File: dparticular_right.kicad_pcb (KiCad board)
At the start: 2 copper layers, 185.7 x 157.2 mm, 51 parts, among them J1 To Left Hand, SW1:10 Key_Ins, SW1:11 Key_Prnt, SW2:10 Key_F7, SW2:11 Key_F8, SW2:12 Key_F9, SW2:13 Key_F10, SW2:14 Key_F11, SW2:15 Key_F12, SW2:16 Key_Del, SW3:10 Key_7, SW3:11 Key_8, SW3:12 Key_9, SW3:13 Key_0, SW3:14 Key_Hyph, SW3:15 Key_Eql, SW3:16 Key_Bksp, SW3:9 Key_6, SW4:10 Key_U, SW4:11 Key_I, SW4:12 Key_O, SW4:13 Key_P, SW4:14 Key_LBrk, SW4:15 Key_RBrk, SW4:16 Key_BkSl, SW4:9 Key_Y, SW5:10 Key_J, SW5:11 Key_K, SW5:12 Key_L, SW5:13 Key_Semi, SW5:14 Key_Quot, SW5:16 Key_Entr, SW5:9 Key_H, SW6:10 Key_M, SW6:11 Key_Coma, SW6:12 Key_Per, SW6:13 Key_Slsh, SW6:14 Key_RShft, SW6:9 Key_N, SW7:11 Key_RAlt, SW7:12 Key_RWin, SW7:13 Key_Menu, SW7:14 Key_RCtrl, SW7:9 Key_RSpc, U1 MCP23018

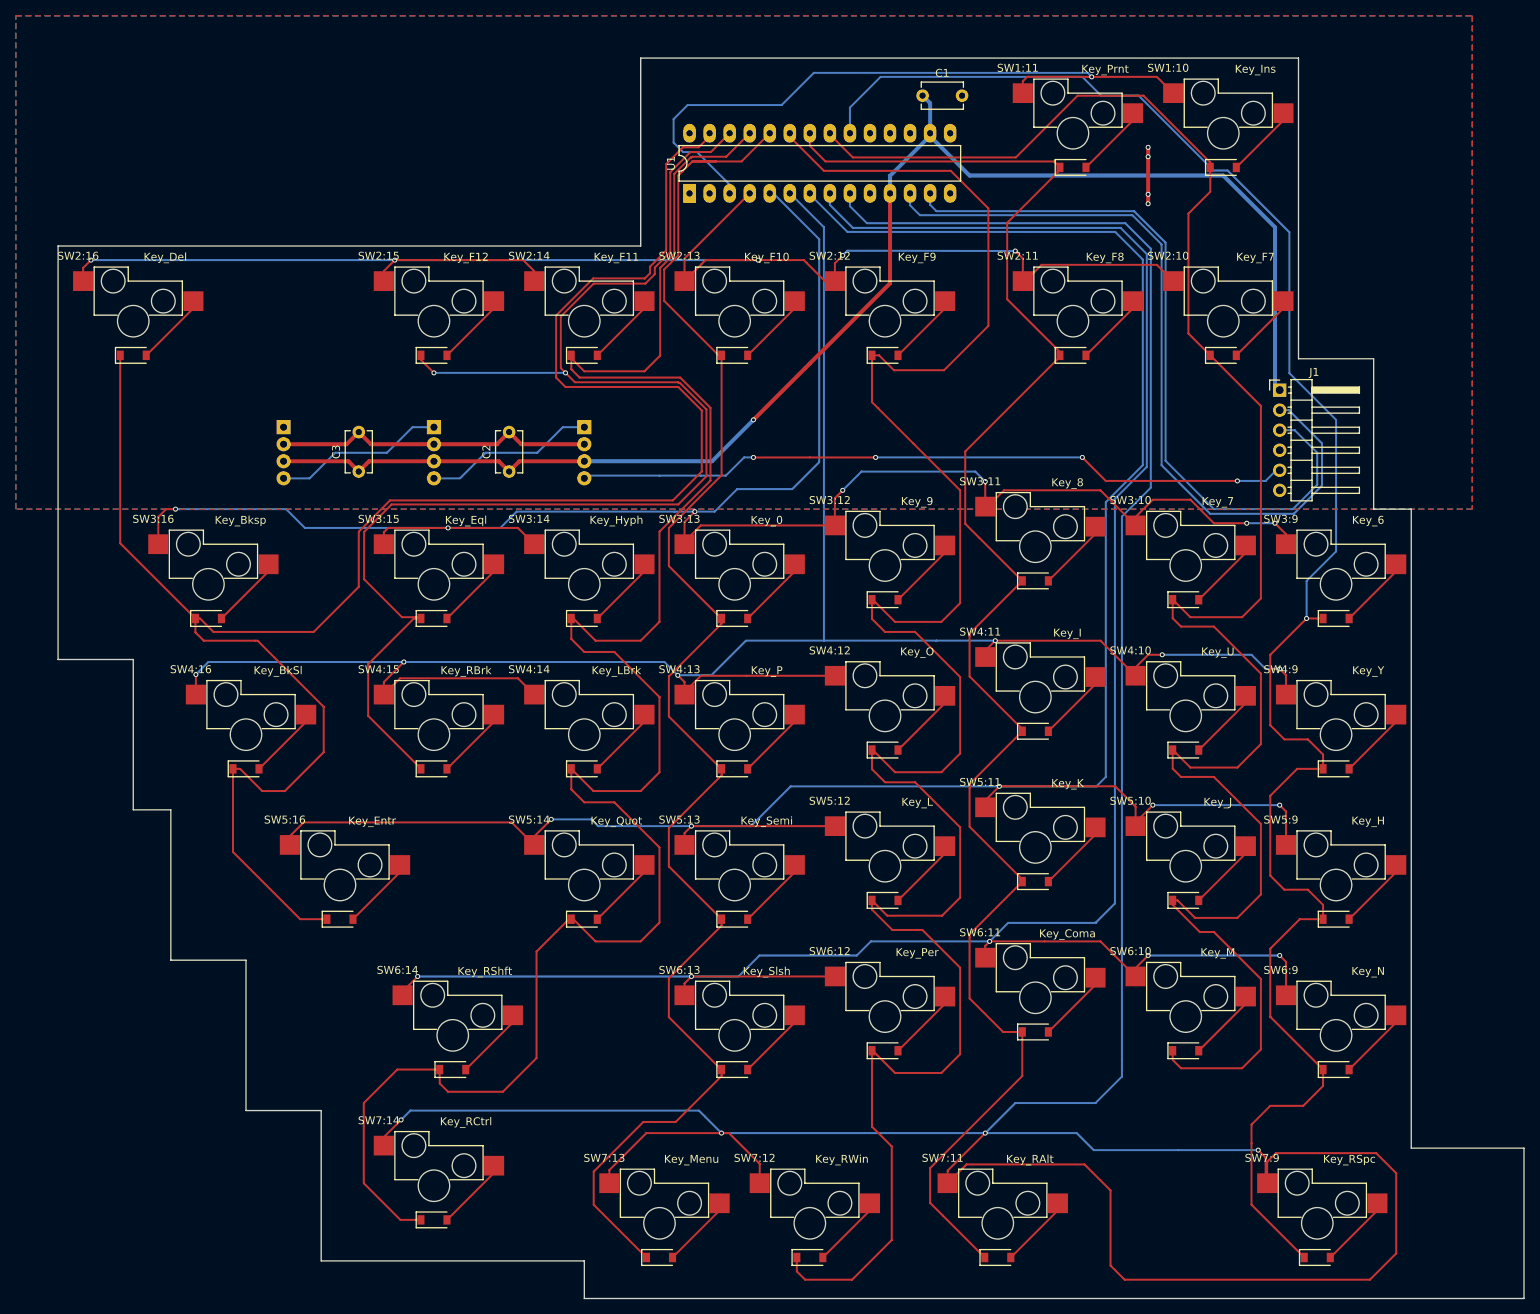
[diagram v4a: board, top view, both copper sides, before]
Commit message: PCBs: Clean up via line by line analysis
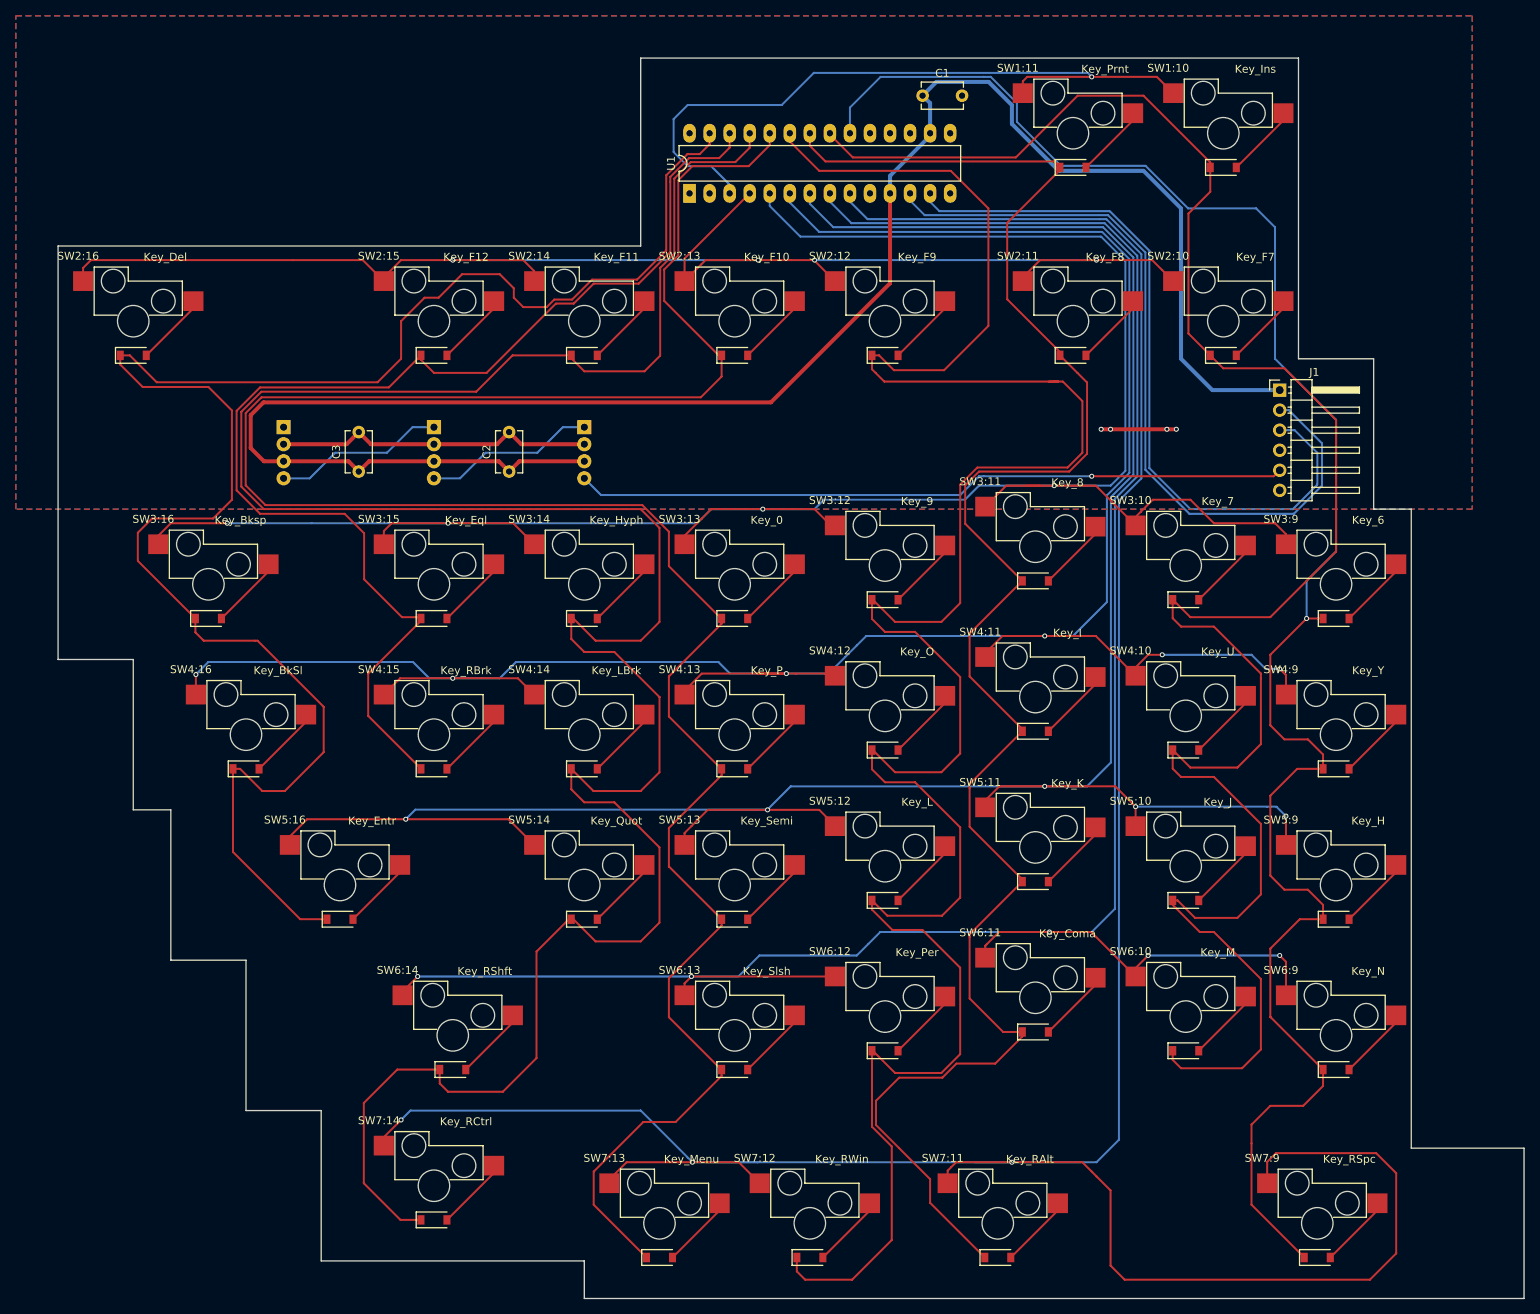
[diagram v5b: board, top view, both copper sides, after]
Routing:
- net /COL13: track 192.0 -> 294.5 mm
- net /COL14: track 259.0 -> 329.8 mm
- net +5V: track 184.3 -> 238.2 mm, vias 1 -> 0
- net /ROW4: track 261.0 -> 310.4 mm
- net /ROW3: track 249.0 -> 295.9 mm, vias 7 -> 4
- net /ROW7: track 425.3 -> 389.2 mm, vias 4 -> 3
- net /COL12: track 270.6 -> 305.5 mm
- net /COL16: track 254.9 -> 227.4 mm
- net /COL15: track 179.3 -> 154.0 mm, vias 2 -> 0
- net /COL11: track 211.8 -> 233.1 mm
- net /COL10: track 245.4 -> 259.9 mm
- net /ROW5: track 294.7 -> 306.9 mm
- net GND: track 47.8 -> 50.2 mm
- net /ROW2: track 197.2 -> 195.6 mm, vias 5 -> 4
- net /ROW6: track 292.8 -> 292.0 mm
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
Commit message: PCBs: Move vias off silk screen
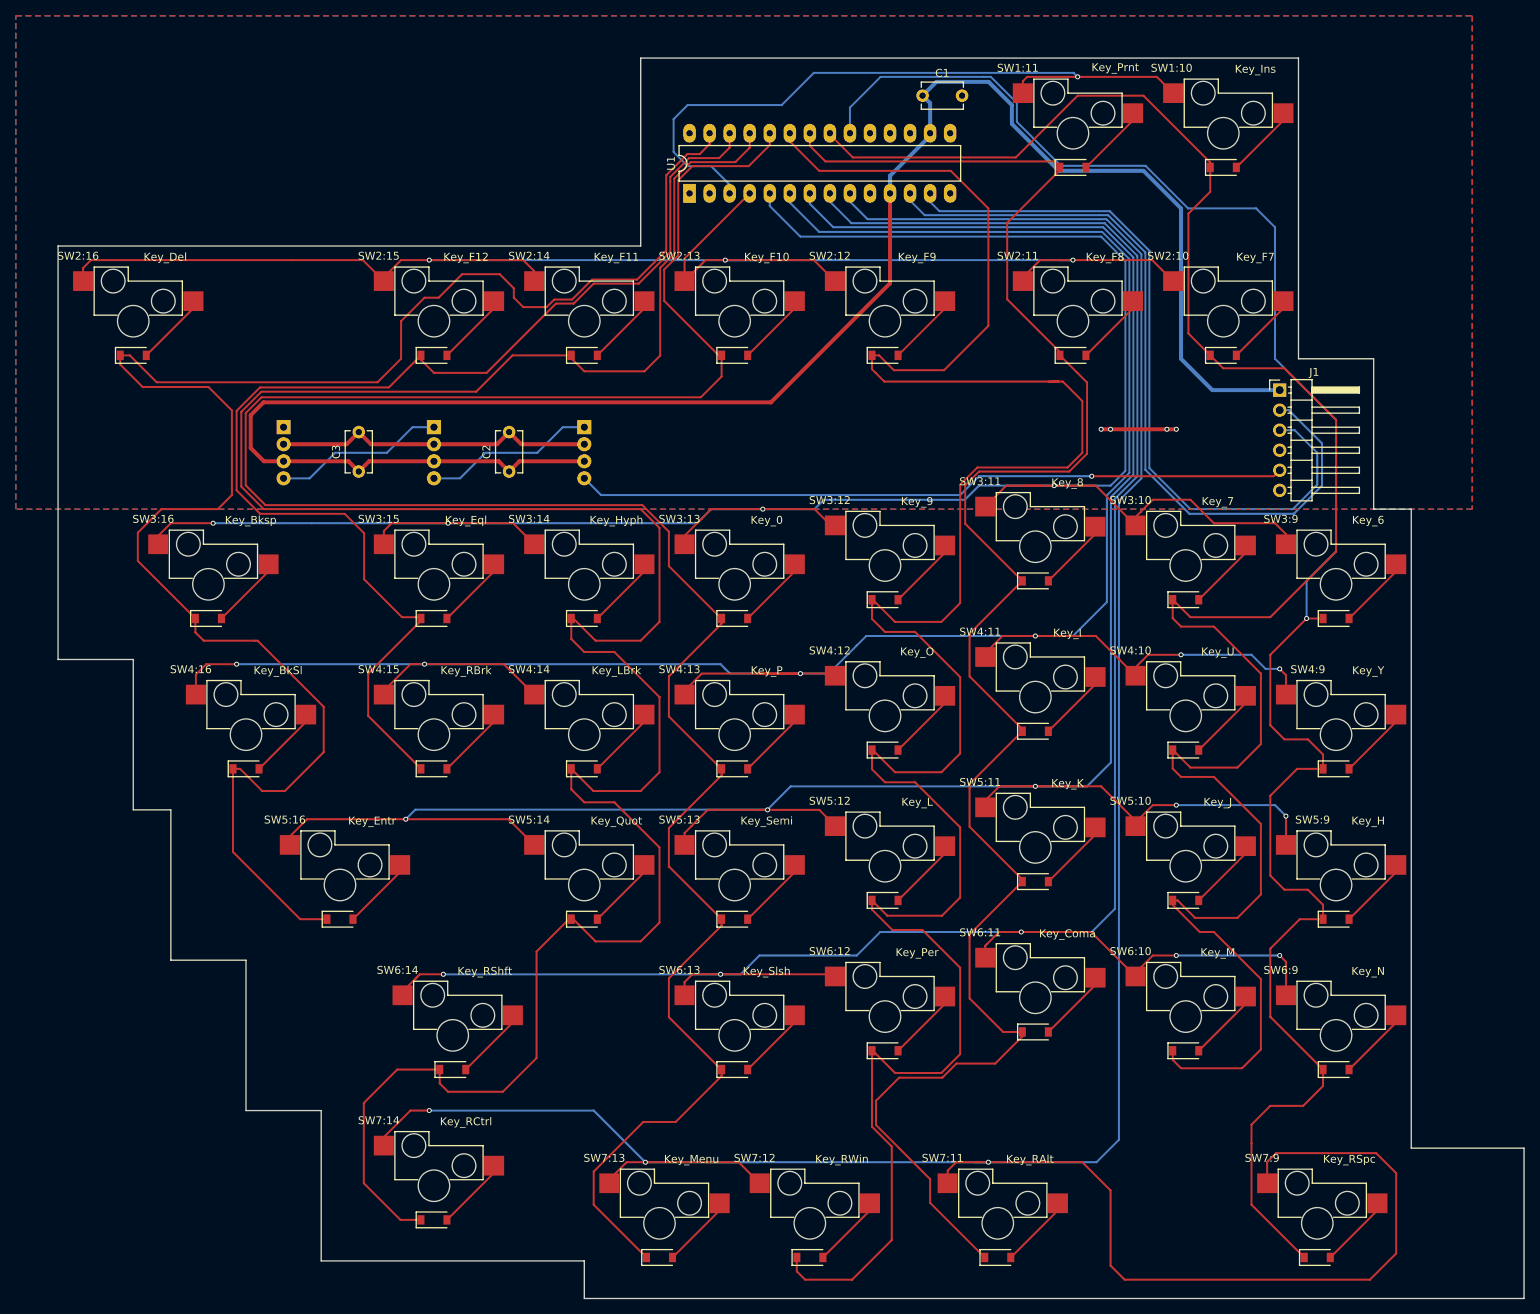
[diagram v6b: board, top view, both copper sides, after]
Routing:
- net /ROW2: track 195.6 -> 214.1 mm, vias 4 -> 3
- net /ROW7: track 389.2 -> 386.2 mm
- net /ROW1: track 91.4 -> 89.6 mm
- net /ROW4: track 310.4 -> 312.0 mm

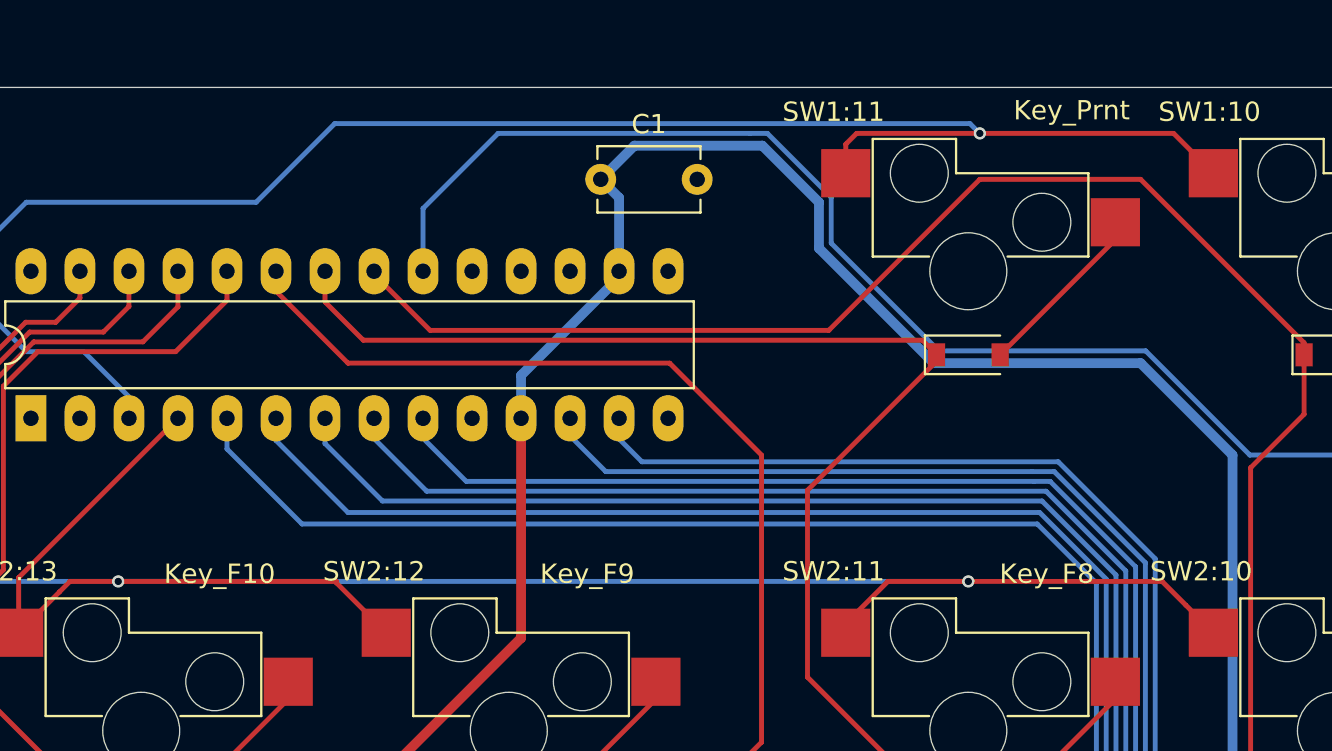
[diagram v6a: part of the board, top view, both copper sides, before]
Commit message: PCBs: More proofreading and cleanup
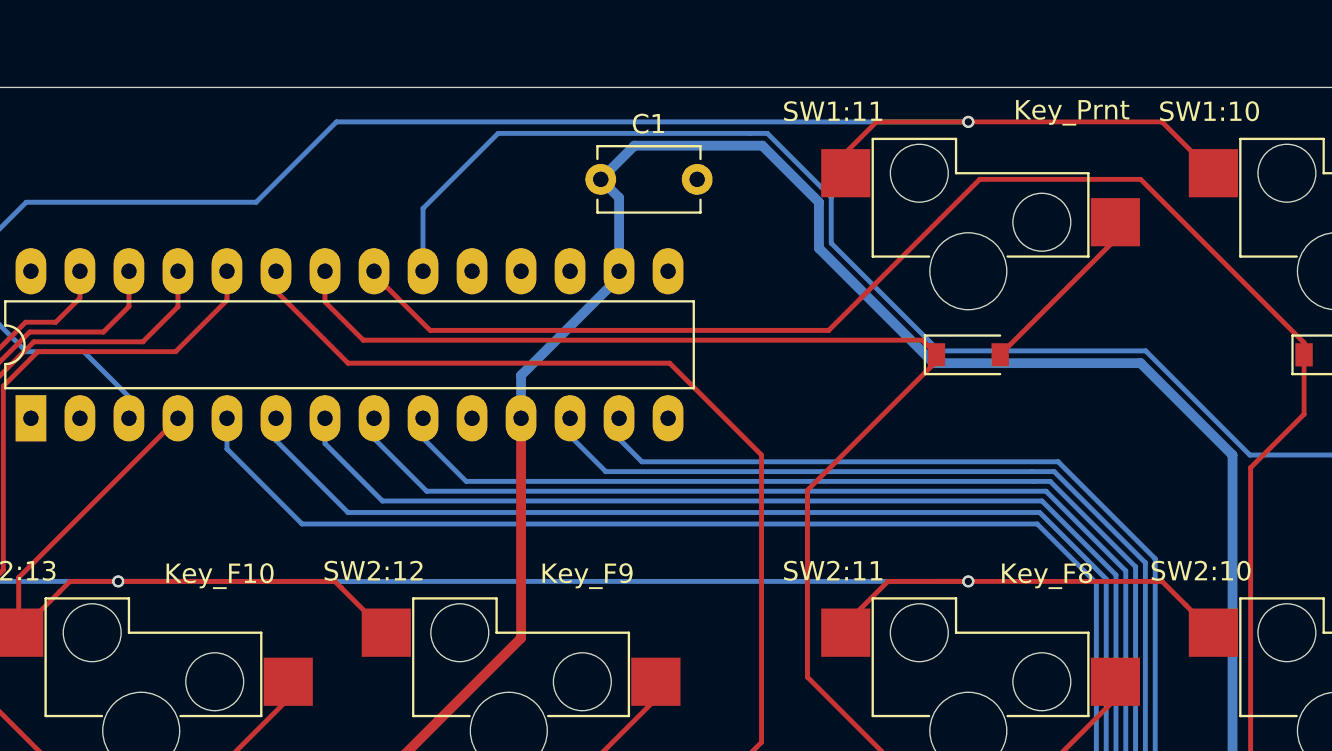
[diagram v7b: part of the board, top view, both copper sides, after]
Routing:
- net /ROW1: track 89.6 -> 89.0 mm

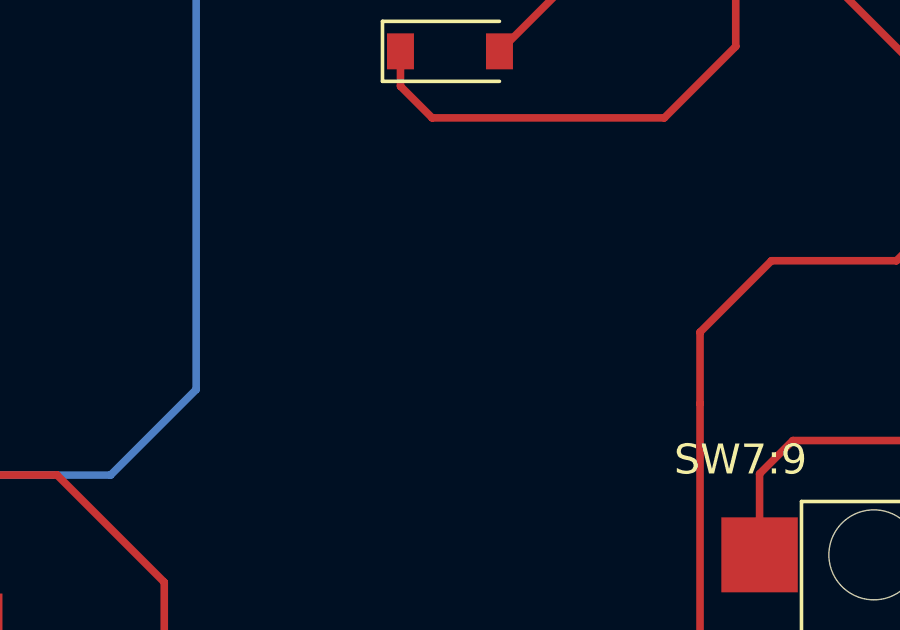
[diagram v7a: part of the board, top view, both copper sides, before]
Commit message: PCBs: Added JLC Order Number placeholders
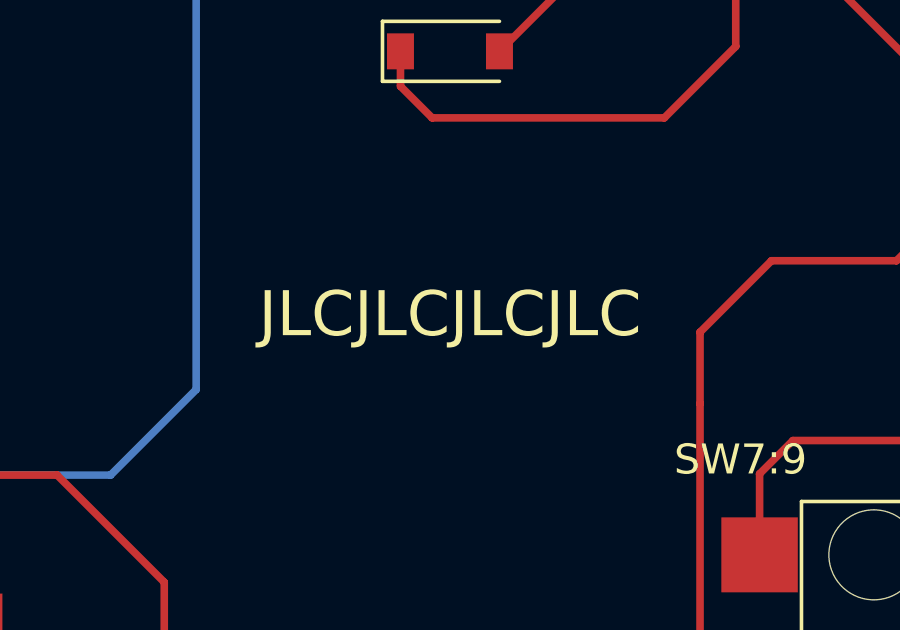
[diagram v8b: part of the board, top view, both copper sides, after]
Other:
- board text added: "JLCJLCJLCJLC"
